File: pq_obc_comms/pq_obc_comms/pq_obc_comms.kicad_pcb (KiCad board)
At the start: 4 copper layers, 40 x 40 mm, 70 parts, among them J1 Conn_01x10, J2 Conn_01x10, J3 Conn_01x10, J4 Conn_01x10, J6 U.FL, U1 STM32L476RGTx, U2 SX1262IMLTRT, U3 BD2232G-GTR, U4 BD2232G-GTR, U5 BGS12PL6E6327XTSA1, U6 BD2232G-GTR, U7 BD2232G-GTR, X1 ECS-120-18-33-JEM-TR3, X2 FA-128_32.0000MF20X-K5, X3 ABS09-32.768KHZ-7-T

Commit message: Functional revision and finishing touches part II
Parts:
- added Annotation1: Silkscreen_Annotation, symbols-nsl:Bike, B.Cu at (140.6, 111.5)
- U5: footprint GGS_RF:PG-TSLP-6-4 -> rf-nsl:PG-TSLP-6-4
- X1: footprint GGS_Miscellaneous:ECX-32 -> miscelaneous-nsl:ECX-32
- X2: footprint GGS_Miscellaneous:EPSON_FA128 -> miscelaneous-nsl:EPSON_FA128
- X3: footprint GGS_Miscellaneous:ABS09 -> miscelaneous-nsl:ABS09
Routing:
- net GND: track 7.40 -> 8.96 mm

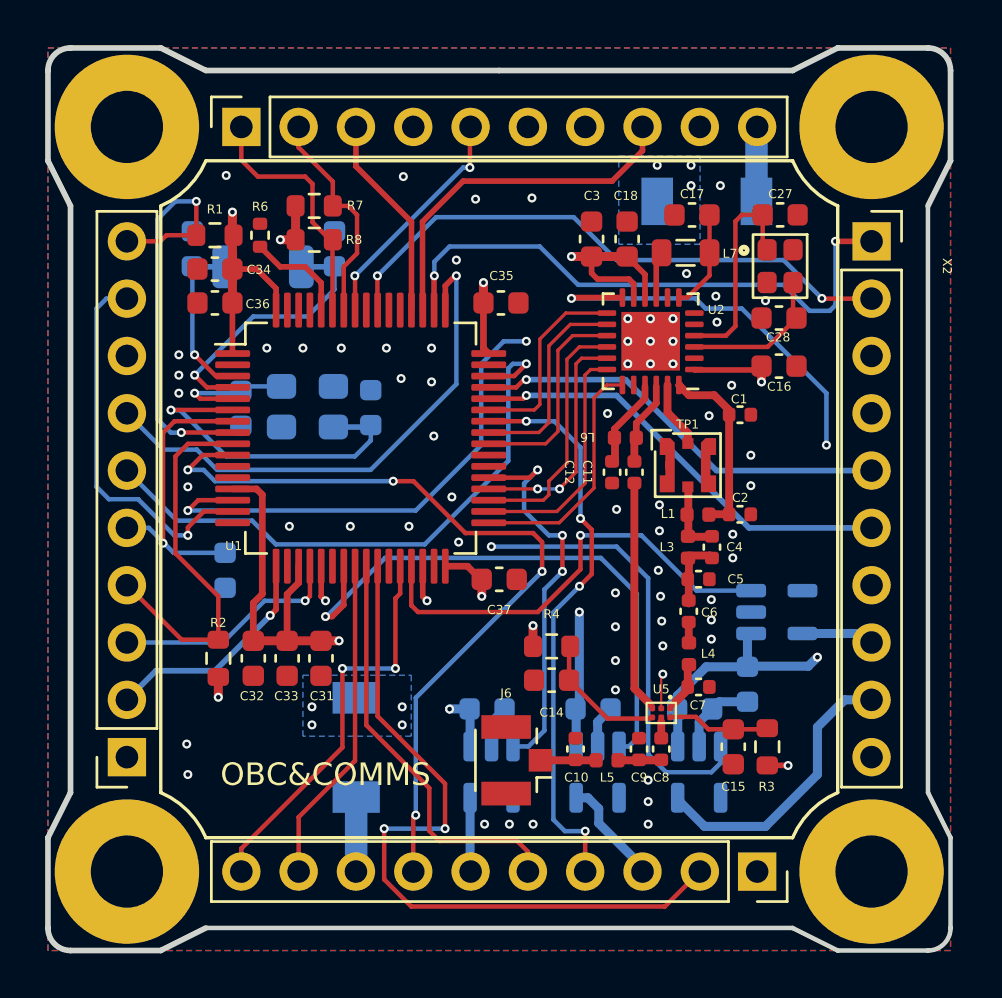
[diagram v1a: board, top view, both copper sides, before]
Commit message: Full Kicad7 transition, library improvement and adaptation, correct footprints and 3D models added
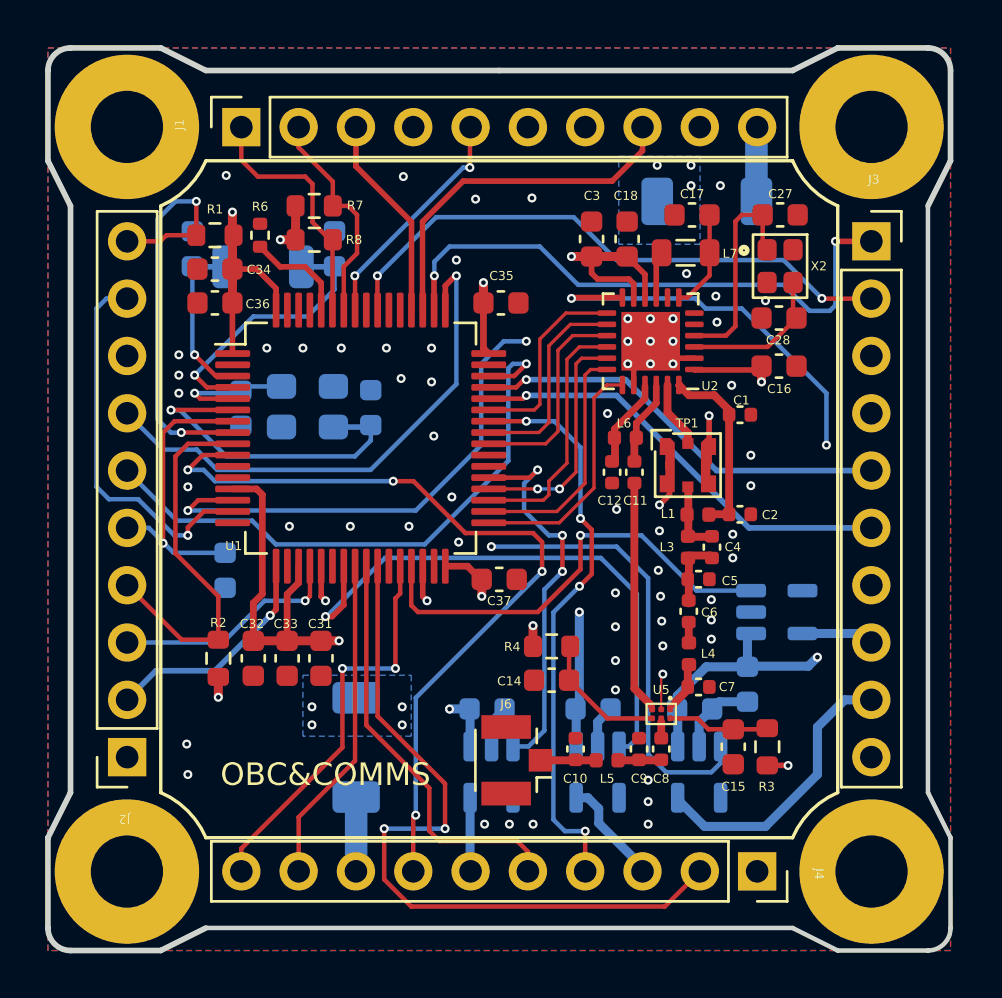
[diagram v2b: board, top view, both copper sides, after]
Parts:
- Annotation1: footprint symbols-nsl:Bike -> -nsl_symbols:Bike
- D1, D2: value RBS1LAM40ATR -> type="D" model="RBS1LAM40ATR" lib=""; footprint Diode_SMD:D_SOD-128 -> -nsl_passive:RBS1LAM40ATR_Schottky
- J1, J2, J3, J4: footprint Connector_PinSocket_2.54mm:PinSocket_1x10_P2.54mm_Vertical -> -nsl_connector:SLW-110-01
- TP1: footprint Connector_Coaxial:CoaxialSwitch_Hirose_MS-156C3_Horizontal -> -nsl_connector:CoaxialSwitch_Hirose_MS-156C3_Horizontal
- U5: footprint rf-nsl:PG-TSLP-6-4 -> -nsl_rf:PG-TSLP-6-4
- X1: footprint miscelaneous-nsl:ECX-32 -> -nsl_miscellaneous:ECX-32
- X2: footprint miscelaneous-nsl:EPSON_FA128 -> -nsl_miscellaneous:EPSON_FA128
- X3: footprint miscelaneous-nsl:ABS09 -> -nsl_miscellaneous:ABS09
- turned D1 to 0 degrees
- turned D2 to -90 degrees
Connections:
- D1 pad 1: 3V3_PERM -> VCC
- D1 pad 2: VCC -> 3V3_PERM
- D2 pad 1: VCC_UMBILICAL -> VCC
- D2 pad 2: VCC -> VCC_UMBILICAL
- U2 pad 23: Net-(TP1-PadC) -> Net-(U2-RFO)
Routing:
- net GND: track 8.96 -> 15.2 mm
- net Net-(U2-RFO): track 0.00 -> 2.97 mm
- net Net-(TP1-PadC): track 2.97 -> 0.00 mm

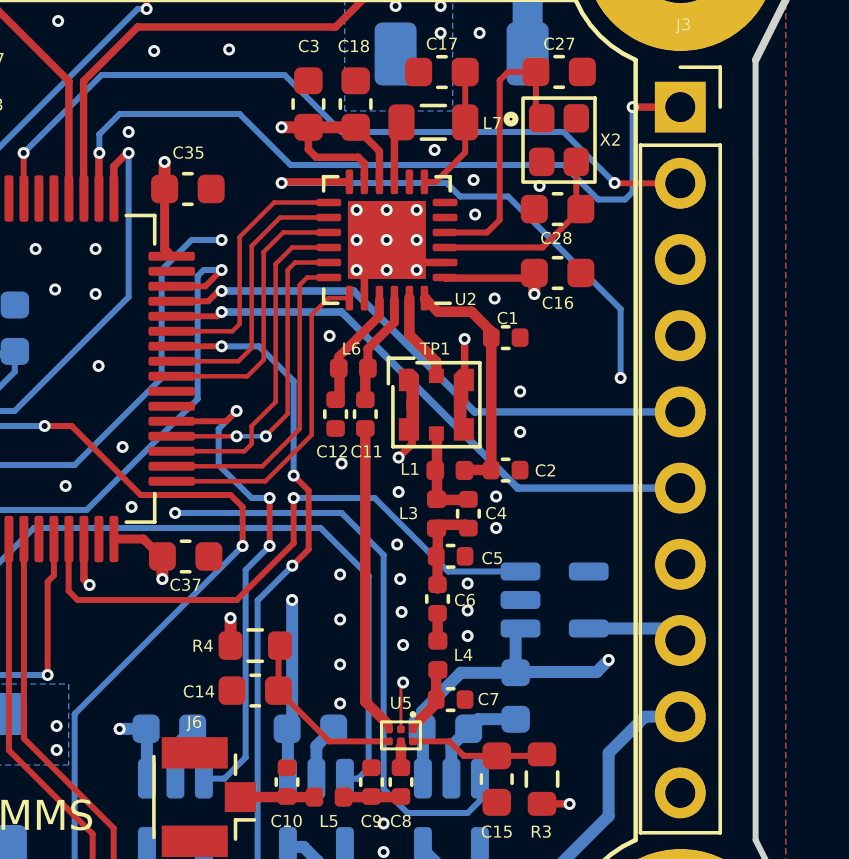
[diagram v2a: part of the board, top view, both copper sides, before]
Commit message: Added adaptive resistive network for battery chemistry and charge voltage flexibility & connected all the PoLs + COMMS to 3V3_perm instead of VCC (3.3V - schottky diode)
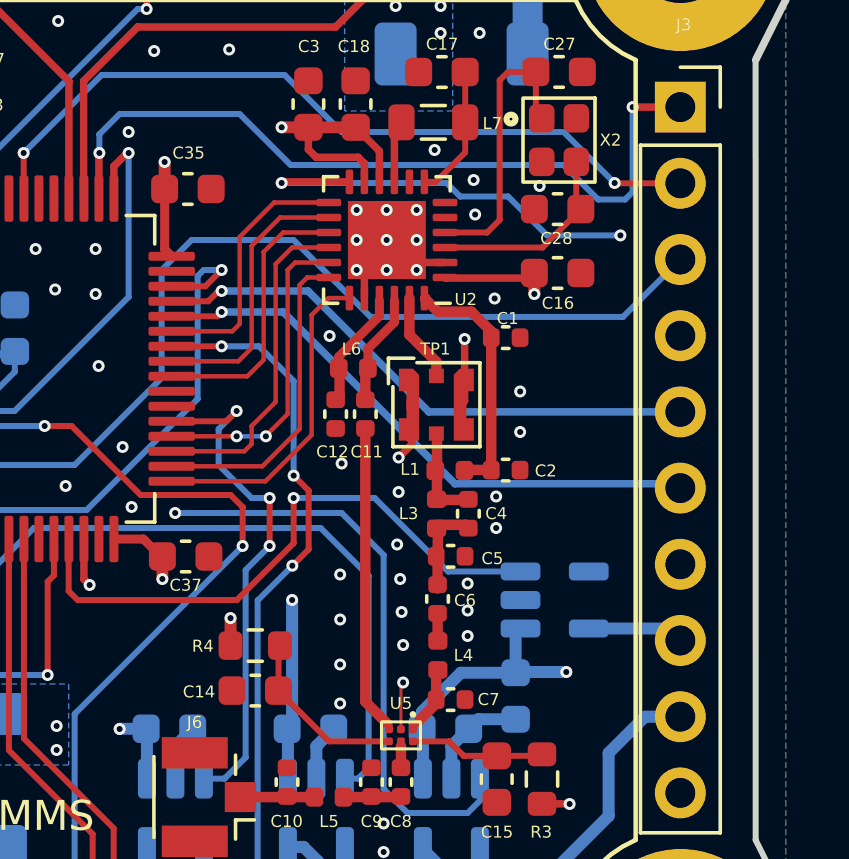
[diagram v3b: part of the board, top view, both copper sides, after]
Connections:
- C13 pad 1: VCC -> 3V3_PERM
- C16 pad 1: VCC -> 3V3_PERM
- C18 pad 1: VCC -> 3V3_PERM
- C3 pad 1: VCC -> 3V3_PERM
- C43 pad 1: VCC -> 3V3_PERM
- C44 pad 1: VCC -> 3V3_PERM
- C45 pad 2: VCC -> 3V3_PERM
- R4 pad 1: VCC -> 3V3_PERM
- U2 pad 1: VCC -> 3V3_PERM
- U2 pad 10: VCC -> 3V3_PERM
- U2 pad 11: VCC -> 3V3_PERM
- U3 pad 1: VCC -> 3V3_PERM
- U4 pad 1: VCC -> 3V3_PERM
- U6 pad 1: VCC -> 3V3_PERM
- U7 pad 1: VCC -> 3V3_PERM
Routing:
- net VCC: track 65.5 -> 33.8 mm, vias 19 -> 13
- net 3V3_PERM: track 3.31 -> 33.5 mm, vias 0 -> 6
- net BATT_NTC: track 41.2 -> 39.5 mm, vias 2 -> 1
- net /DIO2: track 33.4 -> 34.9 mm
- added copper zone on In2.Cu, net 3V3_PERM

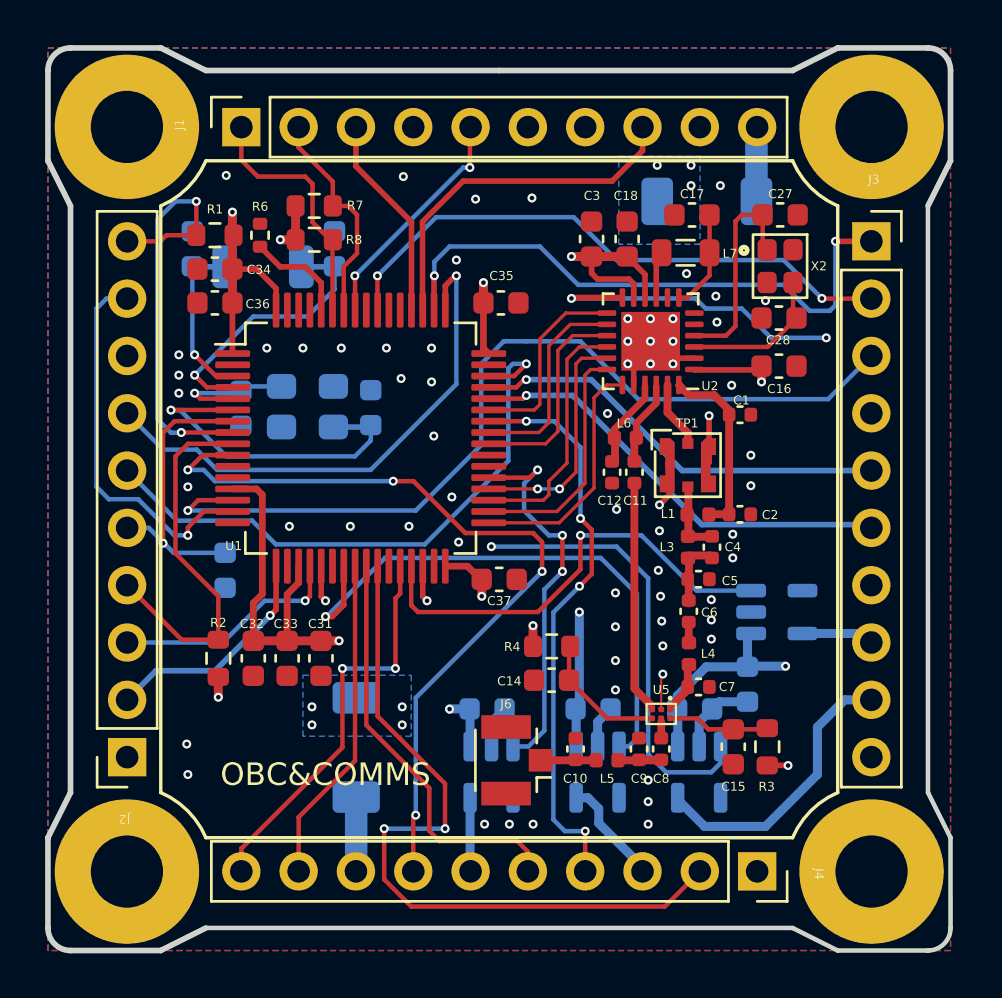
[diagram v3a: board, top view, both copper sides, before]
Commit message: PoL & SX1262 feeding at 3.3V and OBC feeding at 3.1 (Schottky diode) strategy changed from inner layer 2 plane to 1 mm thick traces
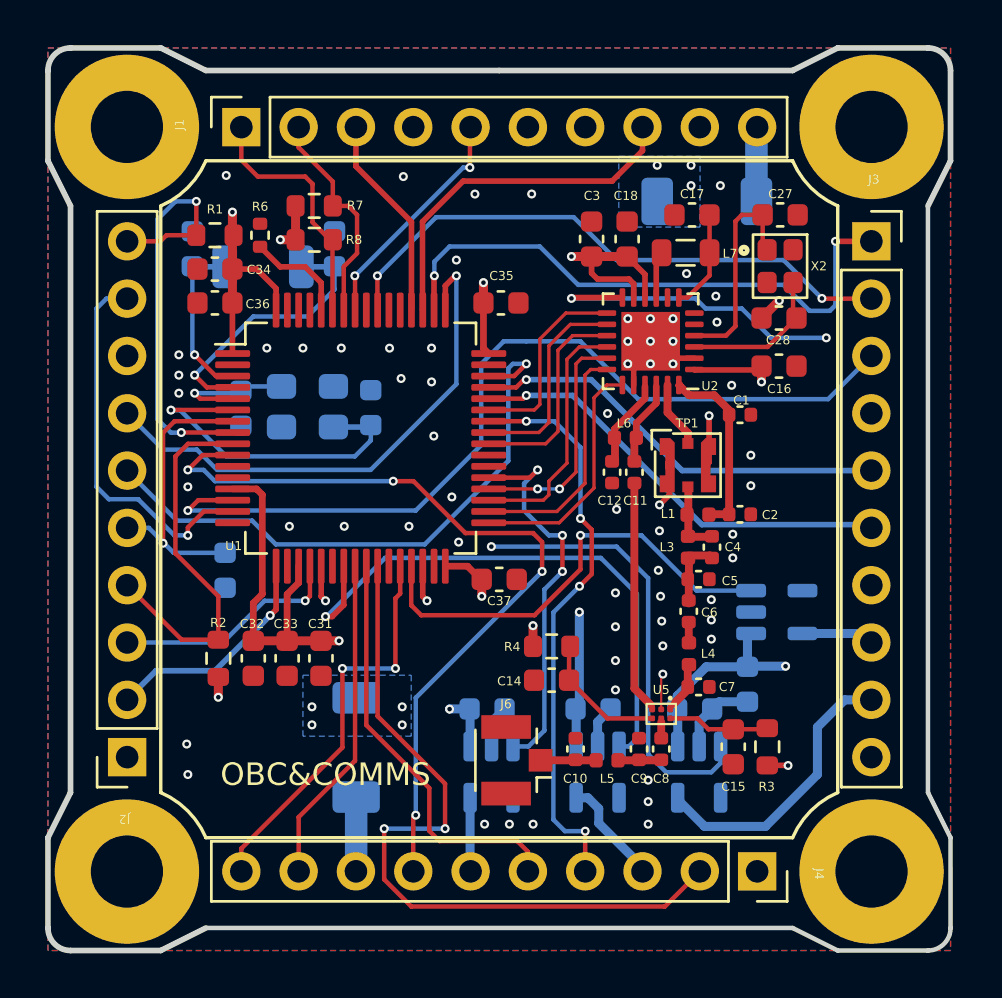
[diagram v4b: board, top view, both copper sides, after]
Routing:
- net VCC: track 33.8 -> 98.2 mm
- net 3V3_PERM: track 33.5 -> 93.1 mm
- net GND: track 15.2 -> 16.3 mm
- removed copper zone on In2.Cu, net 3V3_PERM
